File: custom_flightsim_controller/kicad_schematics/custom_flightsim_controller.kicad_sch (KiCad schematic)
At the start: 9 parts, among them SW4 SW_SPDT_MSM, SW5 SW_SPDT_MSM, SW6 SW_SPDT_MSM, SW7 SW_SPDT_MSM, SW8 SW_Push, U1 Sparkfun_Pro_Micro

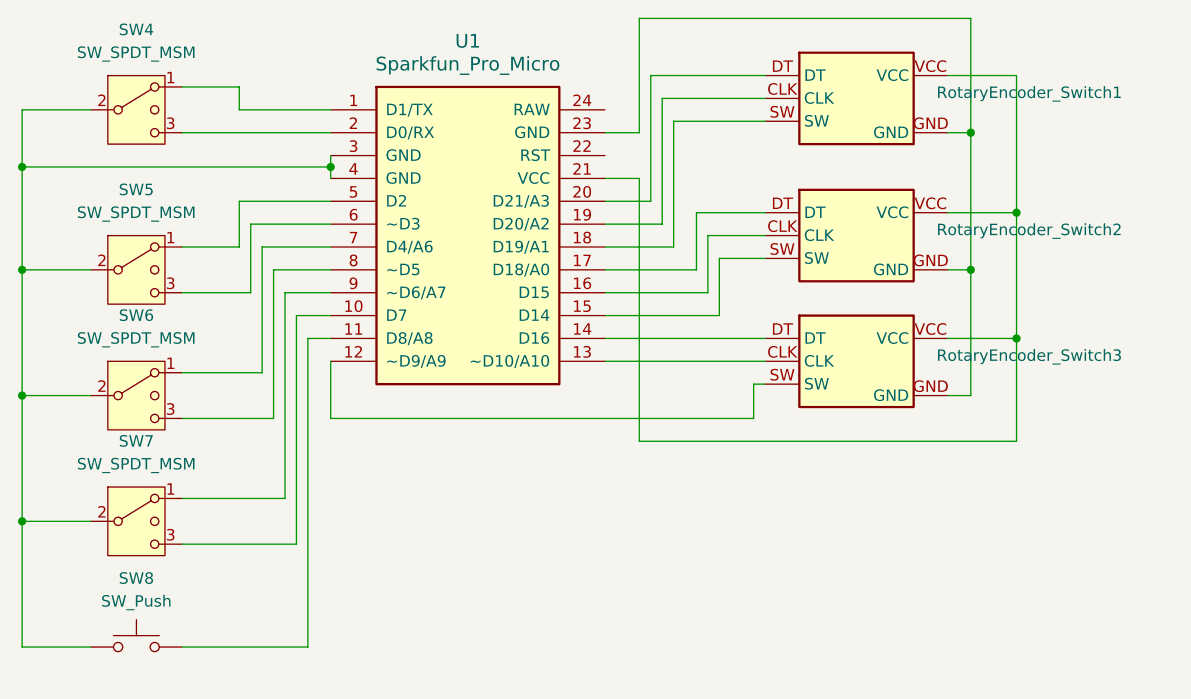
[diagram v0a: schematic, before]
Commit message: Controller: Scheme: Updated schematics to connect SW1 pin with RST on controller
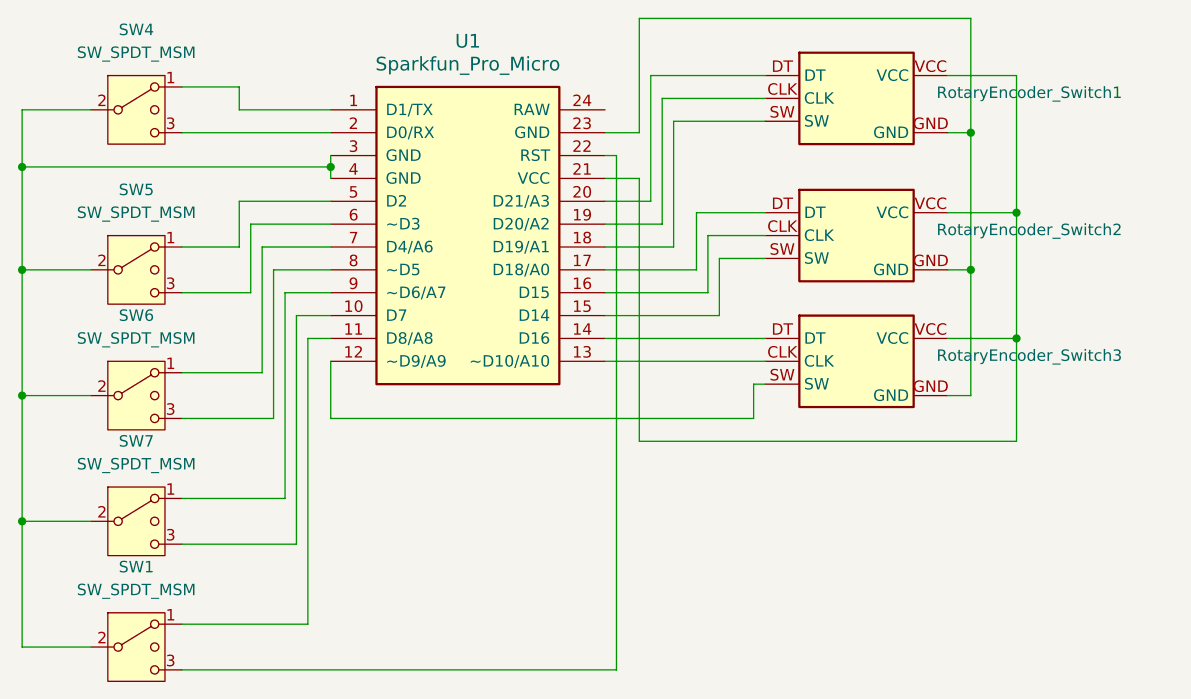
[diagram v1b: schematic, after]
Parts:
- removed SW8: SW_Push, symbol Switch:SW_Push
- added SW1: SW_SPDT_MSM, symbol Switch:SW_SPDT_MSM
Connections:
- net at SW4.2 (3), SW5.2 (3), SW6.2 (3)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: now also SW1.2 (3)
- net at U1.11 (D8/A8): now also SW1.1
- net at U1.22 (RST): now also SW1.3 (4)
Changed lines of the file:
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@@
+	(wire
+		(pts
+			(xy 149.86 55.88) (xy 149.86 113.03)
+		)
+		(stroke
+			(width 0)
+			(type default)
+		)
+	)
 	(wire
 		(pts
@@
 	(wire
 		(pts
+			(xy 148.59 55.88) (xy 149.86 55.88)
+		)
+		(stroke
+			(width 0)
+			(type default)
+		)
+	)
+	(wire
+		(pts
 			(xy 194.31 87.63) (xy 152.4 87.63)
 		)
@@
 	(wire
 		(pts
-			(xy 115.57 110.49) (xy 115.57 76.2)
+			(xy 115.57 107.95) (xy 115.57 76.2)
 		)
 		(stroke
@@
 	(wire
 		(pts
+			(xy 149.86 113.03) (xy 101.6 113.03)
+		)
+		(stroke
+			(width 0)
+			(type default)
+		)
+	)
+	(wire
+		(pts
 			(xy 152.4 58.42) (xy 148.59 58.42)
 		)
@@
 	(wire
 		(pts
-			(xy 101.6 110.49) (xy 115.57 110.49)
+			(xy 101.6 107.95) (xy 115.57 107.95)
 		)
 		(stroke
@@
 	)
 	(symbol
-		(lib_id "Switch:SW_Push")
-		(at 96.52 110.49 0)
-		(unit 1)
-		(exclude_from_sim no)
-		(in_bom yes)
-		(on_board yes)
-		(dnp no)
-		(fields_autoplaced yes)
-		(property "Reference" "SW8"
-			(at 96.52 102.87 0)
-			(effects
-				(font
-					(size 1.27 1.27)
-				)
-			)
-		)
-		(property "Value" "SW_Push"
-			(at 96.52 105.41 0)
-			(effects
-				(font
-					(size 1.27 1.27)
-				)
-			)
-		)
-		(property "Footprint" ""
-			(at 96.52 105.41 0)
-			(effects
-				(font
-					(size 1.27 1.27)
-				)
-				(hide yes)
-			)
-		)
-		(property "Datasheet" "~"
-			(at 96.52 105.41 0)
-			(effects
-				(font
-					(size 1.27 1.27)
-				)
-				(hide yes)
-			)
-		)
-		(property "Description" "Push button switch, generic, two pins"
-			(at 96.52 110.49 0)
-			(effects
-				(font
-					(size 1.27 1.27)
-				)
-				(hide yes)
-			)
-		)
-		(pin "1"
-		)
-		(pin "2"
-		)
-		(instances
-			(project ""
-				(path "/1e0e1b28-f6bb-4218-ab83-9b1d927bd31c"
-					(reference "SW8")
-					(unit 1)
-				)
-			)
-		)
-	)
-	(symbol
 		(lib_id "Arduino:Sparkfun_Pro_Micro")
 		(at 133.35 66.04 0)
@@
 					(unit 1)
 				)
+			)
+		)
+	)
+	(symbol
+		(lib_id "Switch:SW_SPDT_MSM")
+		(at 96.52 110.49 0)
+		(unit 1)
+		(exclude_from_sim no)
+		(in_bom yes)
+		(on_board yes)
+		(dnp no)
+		(fields_autoplaced yes)
+		(property "Reference" "SW1"
+			(at 96.52 101.6 0)
+			(effects
+				(font
+					(size 1.27 1.27)
+				)
+			)
+		)
+		(property "Value" "SW_SPDT_MSM"
+			(at 96.52 104.14 0)
+			(effects
+				(font
+					(size 1.27 1.27)
+				)
+			)
+		)
+		(property "Footprint" ""
+			(at 82.55 99.06 0)
+			(effects
+				(font
+					(size 1.27 1.27)
+				)
+				(hide yes)
+			)
+		)
+		(property "Datasheet" "~"
+			(at 96.52 118.11 0)
+			(effects
+				(font
+					(size 1.27 1.27)
+				)
+				(hide yes)
+			)
+		)
+		(property "Description" "Switch, single pole double throw, center OFF position"
+			(at 96.52 110.49 0)
+			(effects
+				(font
+					(size 1.27 1.27)
+				)
+				(hide yes)
+			)
+		)
+		(pin "1"
+		)
+		(pin "3"
+		)
+		(pin "2"
+		)
+		(instances
+			(project "custom_flightsim_controller"
+				(path "/1e0e1b28-f6bb-4218-ab83-9b1d927bd31c"
+					(reference "SW1")
+					(unit 1)
+				)
